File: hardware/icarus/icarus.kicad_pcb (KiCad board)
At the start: 4 copper layers, 43.7 x 42.4 mm, 32 parts, among them J1 USB_B_Micro, J2 SWJ-DP, J3 PWR, J4 PWM, J5 COMMS, J6 GPIO, SW1 RST, SW2 BOOT, U1 STM32F302C8Tx, U2 AMS1117-3.3, U3 MPU-6050, Y1 12MHz

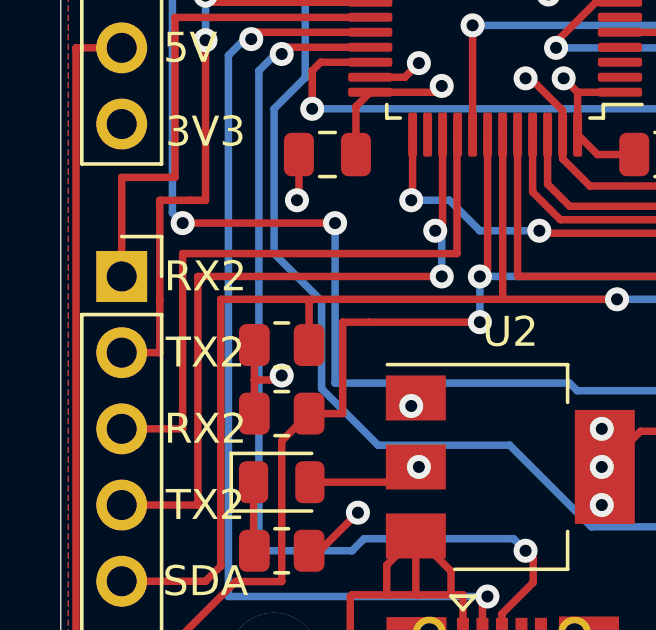
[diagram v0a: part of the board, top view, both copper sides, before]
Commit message: Resolves #2, #9, #10. Test points, USART1 Labels, IMU AD0 pint.
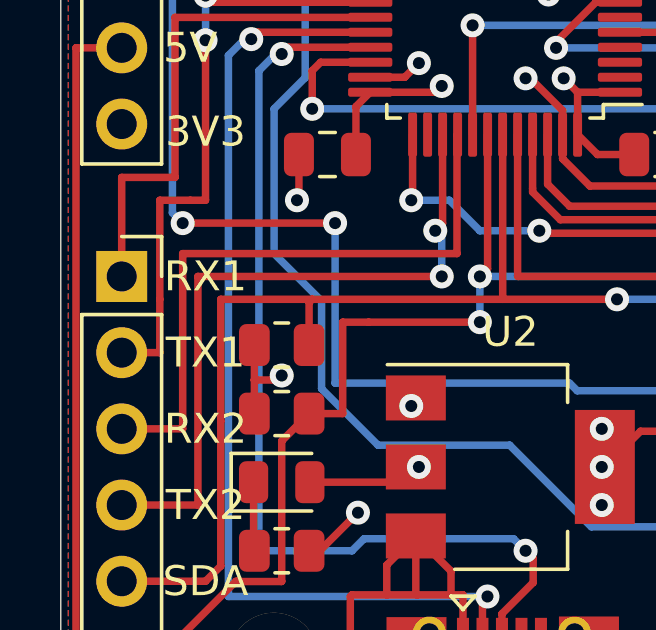
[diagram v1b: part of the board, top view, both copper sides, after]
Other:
- board text added: "RX1"
- board text added: "TX1"

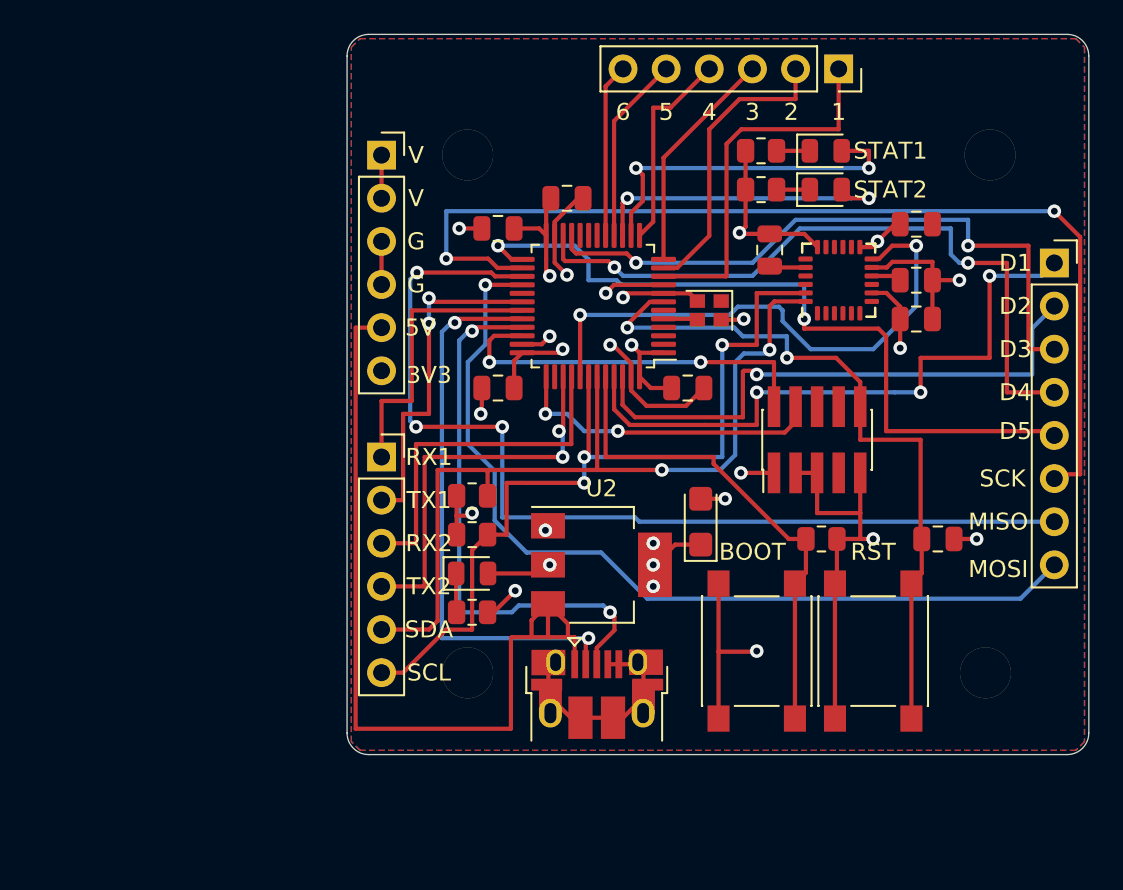
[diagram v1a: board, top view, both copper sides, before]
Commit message: Kicad 6 Update
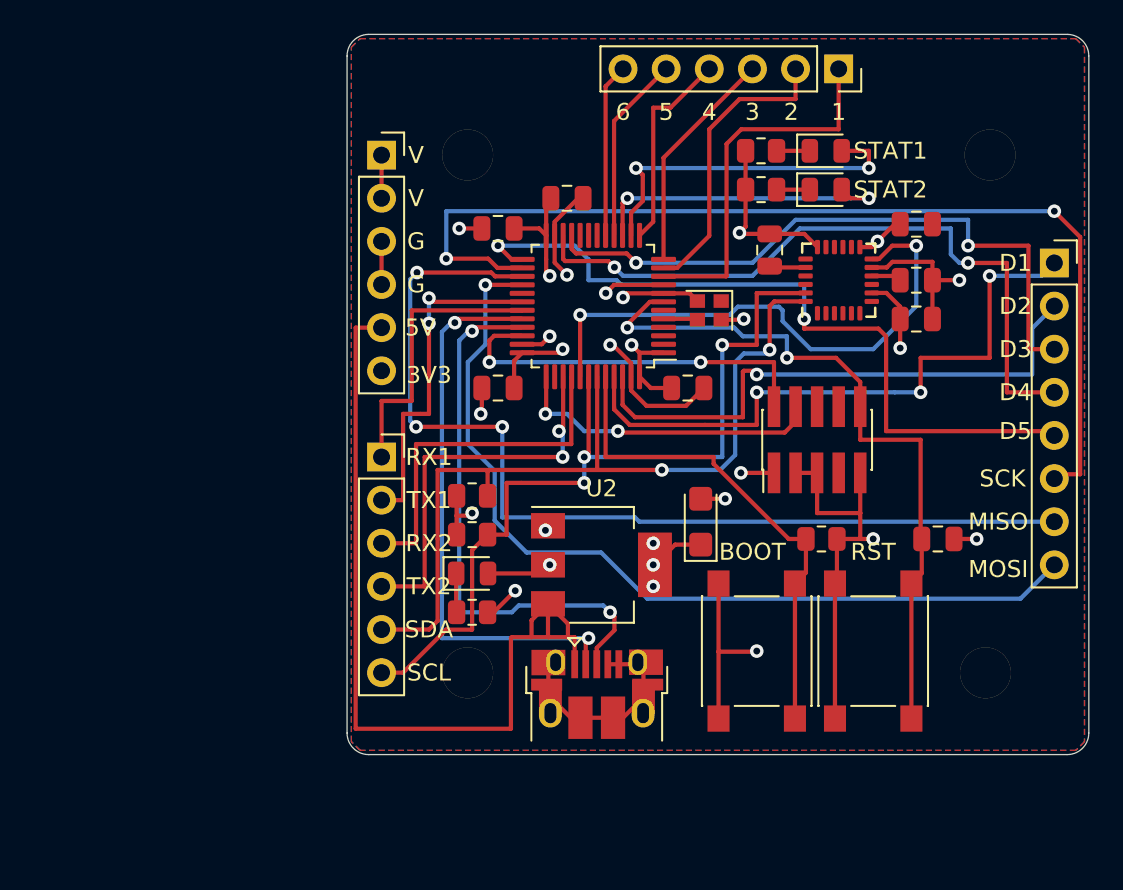
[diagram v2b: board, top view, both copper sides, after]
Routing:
- added copper zone on In1.Cu, net +3V3
- added copper zone on In2.Cu, net GND
- removed copper zone on PWR, net +3V3
- removed copper zone on GND, net GND
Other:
- net class Default removed

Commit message: Resolves #6, #17, #18. Resize and routing. Added barometer.
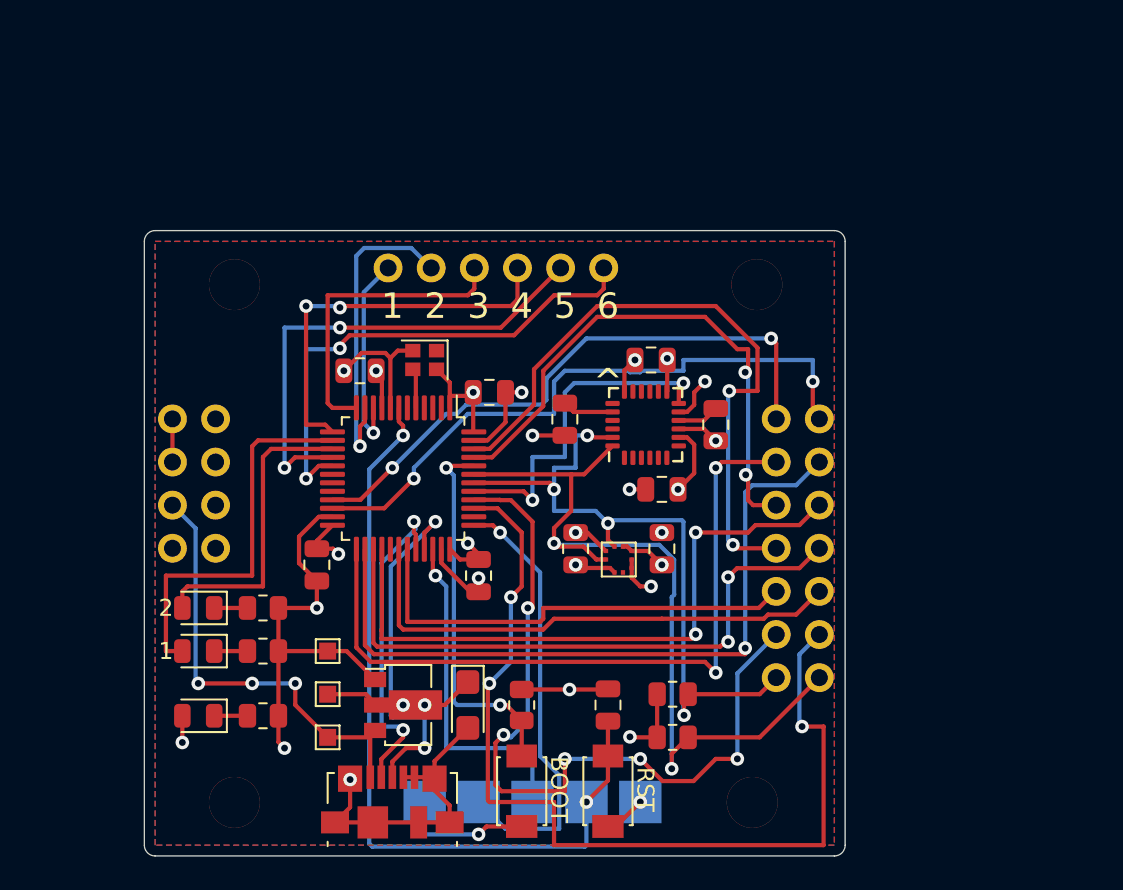
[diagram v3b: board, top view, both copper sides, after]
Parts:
- removed J3: PWR, Connector_PinSocket_2.54mm:PinSocket_1x06_P2.54mm_Vertical
- removed J4: PWM, Connector_PinSocket_2.54mm:PinSocket_1x06_P2.54mm_Vertical
- removed J5: COMMS, Connector_PinSocket_2.54mm:PinSocket_1x06_P2.54mm_Vertical
- removed J6: GPIO, Connector_PinSocket_2.54mm:PinSocket_1x08_P2.54mm_Vertical
- removed REF**: mounting_holes_30.5mm, drone:mounting_holes_30.5mm
- added C12: 100nF, Capacitor_SMD:C_0805_2012Metric, F.Cu at (162.6, 77.8)
- added C2: 100nF, Capacitor_SMD:C_0805_2012Metric, F.Cu at (167.6, 77.8)
- added TP1: 3V3, TestPoint:TestPoint_Pad_1.0x1.0mm, F.Cu at (148.0, 86.4)
- added TP2: 5V, TestPoint:TestPoint_Pad_1.0x1.0mm, F.Cu at (148.0, 88.9)
- added TP3: GND, TestPoint:TestPoint_Pad_1.0x1.0mm, F.Cu at (148.0, 83.8)
- added U4: BMP388, sensors:BMP388, F.Cu at (165.1, 78.4)
- added U5: ICARUS, icarus:icarus-shield, F.Cu at (157.9, 60.0)
- J1: footprint Connector_USB:USB_Micro-B_Amphenol_10103594-0001LF_Horizontal -> Connector_USB:USB_Micro-B_Molex_47346-0001
- J2: value SWJ-DP -> SWD; footprint Connector_PinHeader_1.27mm:PinHeader_2x05_P1.27mm_Vertical_SMD -> custom-breakout:SWD-bcu
- R2, R6, R7: value 100 -> 200
- SW1, SW2: footprint Button_Switch_SMD:SW_Push_1P1T_NO_6x6mm_H9.5mm -> tactile_switches:TS-1088-AR02016
- U2: footprint Package_TO_SOT_SMD:SOT-223-3_TabPin2 -> Package_TO_SOT_SMD:SOT-89-3
- moved D2 47.3 mm to (140.3, 83.8), turned to 180 degrees
- moved D3 44.4 mm to (140.3, 81.3), turned to 180 degrees
- moved R6 41.6 mm to (144.1, 83.8), turned to 0 degrees
- moved R7 38.3 mm to (144.1, 81.3), turned to 0 degrees
- moved J2 27.1 mm to (160.0, 92.7), turned to 0 degrees
- moved C6 26.1 mm to (147.3, 78.7), turned to -90 degrees
- moved C4 21.8 mm to (164.5, 87.0), turned to 90 degrees
- moved C10 21.6 mm to (167.6, 74.3), turned to 0 degrees
- moved C3 20.5 mm to (156.8, 79.4), turned to -90 degrees
- moved R5 20.2 mm to (159.4, 87.0), turned to 90 degrees
- moved C7 19.3 mm to (149.9, 67.3), turned to 180 degrees
- moved R3 18.5 mm to (168.3, 88.9)
- moved D1 18.2 mm to (140.3, 87.6), turned to 180 degrees
- moved SW1 17.7 mm to (164.5, 92.1)
- moved C1 17.5 mm to (156.2, 87.0), turned to -90 degrees
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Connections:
- J2 pad 2: /swdio -> /swclk
- J2 pad 3: GND -> /swdio
- J2 pad 4: /swclk -> /nreset
- U1 pad 18: Net-(U1-Pad18) -> unconnected-(U1-Pad18)
- U1 pad 19: Net-(U1-Pad19) -> unconnected-(U1-Pad19)
- U1 pad 2: Net-(U1-Pad2) -> unconnected-(U1-Pad2)
- U1 pad 20: Net-(U1-Pad20) -> unconnected-(U1-Pad20)
- U1 pad 21: /gpio3 -> /gpio1
- U1 pad 22: /gpio4 -> /gpio2
- U1 pad 25: /gpio5 -> /gpio3
- U1 pad 29: Net-(U1-Pad29) -> unconnected-(U1-Pad29)
- U1 pad 3: Net-(U1-Pad3) -> unconnected-(U1-Pad3)
- U1 pad 38: Net-(U1-Pad38) -> unconnected-(U1-Pad38)
- U1 pad 4: Net-(U1-Pad4) -> unconnected-(U1-Pad4)
- U1 pad 45: /gpio1 -> /can_rx
- U1 pad 46: /gpio2 -> /can_tx
- U3 pad 1: Net-(U3-Pad1) -> unconnected-(U3-Pad1)
- U3 pad 6: Net-(U3-Pad6) -> unconnected-(U3-Pad6)
- U3 pad 7: Net-(U3-Pad7) -> unconnected-(U3-Pad7)
- U3 pad 9: Net-(U3-Pad9) -> GND
- Y1 pad 1: Net-(Y1-Pad1) -> unconnected-(Y1-Pad1)
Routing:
- net /gpio5: track 44.7 -> 0.00 mm, vias 2 -> 0
- net /gpio4: track 41.2 -> 0.00 mm, vias 2 -> 0
- net /can_tx: track 0.00 -> 38.6 mm, vias 0 -> 2
- net /usart2_tx: track 23.3 -> 56.6 mm, vias 2 -> 3
- net /can_rx: track 0.00 -> 32.6 mm, vias 0 -> 2
- net /usart2_rx: track 21.0 -> 46.7 mm, vias 0 -> 5
- net VBUS: track 51.8 -> 26.6 mm, vias 0 -> 3
- net /miso: track 58.7 -> 36.6 mm, vias 3 -> 2
- net /pwm6: track 10.2 -> 29.8 mm, vias 0 -> 2
- net /sck: track 61.1 -> 43.0 mm, vias 2 -> 1
- net /pwm5: track 11.1 -> 29.0 mm, vias 0 -> 2
- net /mosi: track 52.8 -> 38.0 mm, vias 1 -> 2
- net /usb_fs_dm: track 33.6 -> 18.9 mm
- net /imu_int: track 32.6 -> 20.6 mm
- net /usb_fs_dp: track 33.1 -> 21.4 mm
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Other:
- board size 43.7 x 42.4 mm -> 41.3 x 36.8 mm
- board text added: "GND"
- board text added: "NRST"
- board text added: "SWCLK"
- board text added: "SWDIO"
- board text added: "^"
- board text added: "icarus :: Rev B nnarain"
- board text removed: "5V"
- board text removed: "D1"
- board text removed: "D2"
- board text removed: "D3"
- board text removed: "D4"
- board text removed: "D5"
- board text removed: "G"
- board text removed: "MISO"
- board text removed: "MOSI"
- board text removed: "RX1"
- board text removed: "RX2"
- board text removed: "SCK"
- board text removed: "SCL"
- board text removed: "SDA"
- board text removed: "TX1"
- board text removed: "TX2"
- board text removed: "V"
- board text removed: "icarus :: Rev A nnarain"

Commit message: Rev C
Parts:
- removed C11, C12: 100nF, Capacitor_SMD:C_0805_2012Metric
- removed J2: SWD, custom-breakout:SWD-bcu
- removed Y1: 12MHz, Crystal:Crystal_SMD_2016-4Pin_2.0x1.6mm
- added D4: STAT, LED_SMD:LED_WS2812B_PLCC4_5.0x5.0mm_P3.2mm, F.Cu at (140.6, 80.4)
- added D5: CHR, LED_SMD:LED_0805_2012Metric, F.Cu at (142.7, 88.4)
- added G***: LOGO, symbols:battery2_3, F.Cu at (159.9, 86.9)
- added G***: LOGO, icarus:icarus-logo, F.Cu at (136.9, 73.8)
- added G***: LOGO, symbols:charge_1x1, F.Cu at (142.7, 90.7)
- added G***: LOGO, symbols:radio1, B.Cu at (149.1, 52.6)
- added M1: RTR1, Connector_PinHeader_2.54mm:PinHeader_1x02_P2.54mm_Vertical, F.Cu at (163.3, 61.1)
- added M2: RTR2, Connector_PinHeader_2.54mm:PinHeader_1x02_P2.54mm_Vertical, F.Cu at (163.3, 81.9)
- added M3: RTR3, Connector_PinHeader_2.54mm:PinHeader_1x02_P2.54mm_Vertical, F.Cu at (135.1, 61.1)
- added M4: RTR4, Connector_PinHeader_2.54mm:PinHeader_1x02_P2.54mm_Vertical, F.Cu at (135.1, 81.9)
- added P1: USB_C_Plug_USB2.0, USB-C-Connectors:TYPE-C-31-M-04, F.Cu at (149.5, 89.5)
- added Q1: DMG2305, Package_TO_SOT_SMD:SOT-23, F.Cu at (155.2, 79.0)
- added Q2: 2N7002, Package_TO_SOT_SMD:SOT-23, F.Cu at (140.5, 64.9)
- added R1: 100k, Resistor_SMD:R_0402_1005Metric, F.Cu at (158.6, 82.2)
- added R10: 1k, Resistor_SMD:R_0402_1005Metric, F.Cu at (142.9, 85.3)
- added R11: 10k, Resistor_SMD:R_0402_1005Metric, F.Cu at (160.4, 75.7)
- added R12: 10k, Resistor_SMD:R_0402_1005Metric, F.Cu at (160.4, 72.3)
- added R13: 10k, Resistor_SMD:R_0402_1005Metric, F.Cu at (158.4, 66.0)
- added R8: 4.7k, Resistor_SMD:R_0402_1005Metric, F.Cu at (157.6, 76.2)
- added R9: 100k, Resistor_SMD:R_0402_1005Metric, F.Cu at (143.6, 67.3)
- added REF**: mounting_holes_30.5mm, drone:mounting_holes_30.5mm, F.Cu at (149.1, 71.5)
- added TP4: GND, TestPoint:TestPoint_Pad_1.0x1.0mm, F.Cu at (162.7, 91.3)
- added U6: BMP388, sensors:BMP388, F.Cu at (139.4, 57.9)
- added U7: ESP32-C3-MINI-1, Espressif:ESP32-C3-MINI-1, F.Cu at (149.1, 60.8)
- C10: value 10nF -> 100nF; footprint Capacitor_SMD:C_0805_2012Metric -> Capacitor_SMD:C_0402_1005Metric
- C2, C5, C7, C8: footprint Capacitor_SMD:C_0805_2012Metric -> Capacitor_SMD:C_0402_1005Metric
- C3: value 4.7uF -> 2.2nF; footprint Capacitor_SMD:C_0805_2012Metric -> Capacitor_SMD:C_0402_1005Metric
- C4: value 100nF -> 10nF; footprint Capacitor_SMD:C_0805_2012Metric -> Capacitor_SMD:C_0402_1005Metric
- C6: value 100nF -> 4.7uF; footprint Capacitor_SMD:C_0805_2012Metric -> Capacitor_SMD:C_0402_1005Metric
- C9: value 2.2nF -> 100nF; footprint Capacitor_SMD:C_0805_2012Metric -> Capacitor_SMD:C_0402_1005Metric
- D1: value PWR -> B5819W; footprint LED_SMD:LED_0805_2012Metric -> Diode_SMD:D_SOD-123
- D2: value STAT1 -> 5V
- D3: value STAT2 -> 3V3
- J1: value USB_B_Micro -> BAT; footprint Connector_USB:USB_Micro-B_Molex_47346-0001 -> Connector_PinHeader_2.54mm:PinHeader_1x02_P2.54mm_Vertical
- R2, R7: value 200 -> 10k; footprint Resistor_SMD:R_0805_2012Metric -> Resistor_SMD:R_0402_1005Metric
- R3: footprint Resistor_SMD:R_0805_2012Metric -> Resistor_SMD:R_0402_1005Metric
- R4: value 10k -> 1k; footprint Resistor_SMD:R_0805_2012Metric -> Resistor_SMD:R_0402_1005Metric
- R5: value 10k -> 560; footprint Resistor_SMD:R_0805_2012Metric -> Resistor_SMD:R_0402_1005Metric
- R6: value 200 -> 6.8k; footprint Resistor_SMD:R_0805_2012Metric -> Resistor_SMD:R_0402_1005Metric
- SW1: value RST -> USER
- SW2: value BOOT -> RST
- TP1: value 3V3 -> VBUS
- TP2: value 5V -> BATT
- U1: value STM32F302C8Tx -> AMS1117-3.3; footprint Package_QFP:LQFP-48_7x7mm_P0.5mm -> Package_TO_SOT_SMD:SOT-223-3_TabPin2
- U2: value AMS1117-3.3 -> DRV8837; footprint Package_TO_SOT_SMD:SOT-89-3 -> Package_SON:WSON-8-1EP_2x2mm_P0.5mm_EP0.9x1.6mm
- U3: value MPU-6050 -> DRV8837; footprint Sensor_Motion:InvenSense_QFN-24_4x4mm_P0.5mm -> Package_SON:WSON-8-1EP_2x2mm_P0.5mm_EP0.9x1.6mm
- U4: value BMP388 -> MPU-6050; footprint sensors:BMP388 -> Sensor_Motion:InvenSense_QFN-24_4x4mm_P0.5mm
- U5: value ICARUS -> MCP73831-2-OT; footprint icarus:icarus-shield -> Package_TO_SOT_SMD:SOT-23-5
- moved R3 39.9 mm to (141.6, 59.2), turned to 90 degrees
- moved C8 34.1 mm to (139.8, 56.3), turned to 180 degrees
- moved R4 29.7 mm to (138.6, 85.3), turned to 90 degrees
- moved U2 27.2 mm to (133.9, 67.1)
- moved C2 22.9 mm to (145.2, 73.4), turned to -90 degrees
- moved R6 22.6 mm to (140.4, 61.6), turned to 90 degrees
- moved C4 22.5 mm to (145.2, 75.4)
- moved R2 20.4 mm to (145.7, 67.3)
- moved SW1 20.3 mm to (164.7, 71.8), turned to 180 degrees
- moved R7 19.9 mm to (141.6, 61.6), turned to -90 degrees
- moved R5 18.7 mm to (140.7, 85.3)
- moved U4 17.4 mm to (149.1, 71.5), turned to -90 degrees
- moved SW2 16.7 mm to (164.7, 76.2), turned to 0 degrees
- moved D1 16.1 mm to (155.6, 82.3), turned to 0 degrees
- moved U5 14.9 mm to (155.2, 74.7), turned to -90 degrees
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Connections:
- C10 pad 1: GND -> /user_btn
- C10 pad 2: +3V3 -> GND
- C2 pad 1: +3V3 -> Net-(C2-Pad1)
- C3 pad 1: +3V3 -> Net-(C3-Pad1)
- C4 pad 1: /nreset -> GND
- C4 pad 2: GND -> +3V3
- C5 pad 1: +3V3 -> GND
- C5 pad 2: GND -> +3V3
- C6 pad 1: +3V3 -> +BATT
- C8 pad 1: Net-(C8-Pad1) -> +3V3
- C9 pad 1: Net-(C9-Pad1) -> /nreset
- D1 pad 2: +3V3 -> VBUS
- D2 pad 2: /led1 -> VBUS
- D3 pad 2: /led2 -> +3V3
- J1 pad 1: VBUS -> +BATT
- J1 pad 2: /usb_fs_dm -> GND
- R2 pad 1: Net-(D1-Pad1) -> /sda
- R2 pad 2: GND -> +3V3
- R3 pad 1: +3V3 -> /scl
- R3 pad 2: /sda -> +3V3
- R4 pad 1: +3V3 -> Net-(D2-Pad1)
- R4 pad 2: /scl -> GND
- R5 pad 1: /boot0 -> Net-(D3-Pad1)
- R6 pad 1: Net-(D2-Pad1) -> +BATT
- R6 pad 2: GND -> Net-(R6-Pad2)
- R7 pad 1: Net-(D3-Pad1) -> Net-(R6-Pad2)
- SW1 pad 1: /nreset -> GND
- SW1 pad 2: GND -> /user_btn
- SW2 pad 1: /boot0 -> /nreset
- SW2 pad 2: +3V3 -> GND
- TP1 pad 1: +3V3 -> VBUS
- TP2 pad 1: VBUS -> +BATT
- TP3 pad 1: GND -> +3V3
- U1 pad 1: +3V3 -> GND
- U1 pad 2: unconnected-(U1-Pad2) -> +3V3
- U1 pad 3: unconnected-(U1-Pad3) -> Net-(D1-Pad1)
- U2 pad 1: GND -> +BATT
- U2 pad 2: +3V3 -> Net-(M4-Pad2)
- U2 pad 3: VBUS -> Net-(M3-Pad2)
- U3 pad 1: unconnected-(U3-Pad1) -> +BATT
- U3 pad 2: (no net) -> Net-(M2-Pad2)
- U3 pad 3: (no net) -> Net-(M1-Pad2)
- U3 pad 4: (no net) -> GND
- U3 pad 5: (no net) -> /rtrctl1
- U3 pad 6: unconnected-(U3-Pad6) -> /rtrctl2
- U3 pad 7: unconnected-(U3-Pad7) -> Net-(U3-Pad7)
- U4 pad 1: +3V3 -> unconnected-(U4-Pad1)
- U4 pad 10: +3V3 -> Net-(C2-Pad1)
- U4 pad 2: /scl -> (no net)
- U4 pad 3: GND -> (no net)
- U4 pad 4: /sda -> (no net)
- U4 pad 5: +3V3 -> (no net)
- U4 pad 6: +3V3 -> unconnected-(U4-Pad6)
- U4 pad 8: GND -> +3V3
- U5 pad 1: VDC -> Net-(D5-Pad1)
- U5 pad 3: VDC -> +BATT
- U5 pad 4: GND -> VBUS
- U5 pad 5: VBUS -> Net-(R8-Pad1)
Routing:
- net Net-(D5-Pad1): track 0.00 -> 71.9 mm, vias 0 -> 8
- net /usart2_tx: track 56.6 -> 0.00 mm, vias 3 -> 0
- net Net-(D4-Pad4): track 0.00 -> 47.3 mm, vias 0 -> 2
- net /usb_dm: track 0.00 -> 47.2 mm, vias 0 -> 4
- net /usart2_rx: track 46.7 -> 0.00 mm, vias 5 -> 0
- net /usb_dp: track 0.00 -> 45.2 mm, vias 0 -> 4
- net /gpio3: track 43.3 -> 0.00 mm, vias 2 -> 0
- net /sck: track 43.0 -> 0.00 mm, vias 1 -> 0
- net /can_tx: track 38.6 -> 0.00 mm, vias 2 -> 0
- net /mosi: track 38.0 -> 0.00 mm, vias 2 -> 0
- net /gpio2: track 37.5 -> 0.00 mm, vias 2 -> 0
- net /miso: track 36.6 -> 0.00 mm, vias 2 -> 0
- net VBUS: track 26.6 -> 62.3 mm, vias 3 -> 0
- net /gpio1: track 35.4 -> 0.00 mm, vias 2 -> 0
- net /can_rx: track 32.6 -> 0.00 mm, vias 2 -> 0
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- added copper zone on In1.Cu, net +BATT
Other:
- board size 41.3 x 36.8 mm -> 37.1 x 43.3 mm
- board text added: "B"
- board text added: "G"
- board text added: "RST"
- board text added: "U"
- board text added: "USER"
- board text added: "icarus :: Rev C nnarain"
- board text removed: "1"
- board text removed: "2"
- board text removed: "3V3"
- board text removed: "4"
- board text removed: "5"
- board text removed: "6"
- board text removed: "GND"
- board text removed: "NRST"
- board text removed: "SWCLK"
- board text removed: "SWDIO"
- board text removed: "^"
- board text removed: "icarus :: Rev B nnarain"

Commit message: Rev D
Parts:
- removed C6: 4.7uF, Capacitor_SMD:C_0402_1005Metric
- removed D5: CHR, LED_SMD:LED_0805_2012Metric
- removed the G*** at (142.7, 90.7)
- removed M1: RTR1, Connector_PinHeader_2.54mm:PinHeader_1x02_P2.54mm_Vertical
- removed M2: RTR2, Connector_PinHeader_2.54mm:PinHeader_1x02_P2.54mm_Vertical
- removed M3: RTR3, Connector_PinHeader_2.54mm:PinHeader_1x02_P2.54mm_Vertical
- removed M4: RTR4, Connector_PinHeader_2.54mm:PinHeader_1x02_P2.54mm_Vertical
- removed Q2: 2N7002, Package_TO_SOT_SMD:SOT-23
- removed R10: 1k, Resistor_SMD:R_0402_1005Metric
- removed R7: 10k, Resistor_SMD:R_0402_1005Metric
- removed R8: 4.7k, Resistor_SMD:R_0402_1005Metric
- removed R9: 100k, Resistor_SMD:R_0402_1005Metric
- removed U3: DRV8837, Package_SON:WSON-8-1EP_2x2mm_P0.5mm_EP0.9x1.6mm
- removed U5: MCP73831-2-OT, Package_TO_SOT_SMD:SOT-23-5
- added J2: IO, Connector_PinHeader_2.54mm:PinHeader_1x06_P2.54mm_Vertical, F.Cu at (132.7, 65.2)
- added J3: I2C_EX, Connector_PinHeader_2.54mm:PinHeader_1x02_P2.54mm_Vertical, F.Cu at (164.5, 61.0)
- added J4: UART, Connector_PinHeader_2.54mm:PinHeader_1x02_P2.54mm_Vertical, F.Cu at (164.5, 67.3)
- R6: value 6.8k -> 10k
- U2: value DRV8837 -> BMM150; footprint Package_SON:WSON-8-1EP_2x2mm_P0.5mm_EP0.9x1.6mm -> Package_CSP:WLCSP-12_1.56x1.56mm_P0.4mm
- moved U2 21.2 mm to (154.6, 71.5), turned to 180 degrees
- moved R6 18.8 mm to (156.3, 71.5), turned to -90 degrees
- moved C9 6.00 mm to (160.7, 82.8)
- moved R11 6.00 mm to (160.7, 81.7)
- moved SW2 5.84 mm to (164.7, 82.0)
- moved R13 5.34 mm to (153.3, 67.7)
- moved C10 5.23 mm to (159.9, 76.3)
- moved R12 5.23 mm to (159.9, 77.5)
- moved SW1 5.08 mm to (164.7, 76.8)
- moved G*** 4.50 mm to (140.3, 70.9), turned to 90 degrees
- moved C2 1.85 mm to (145.7, 71.6)
- moved C4 1.85 mm to (145.7, 73.7)
- moved C5 1.85 mm to (145.7, 69.6)
- moved D3 1.73 mm to (142.4, 88.4)
- moved R5 1.65 mm to (142.4, 85.3)
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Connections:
- net /rtrctl1 renamed Net-(R13-Pad2)
- R6 pad 1: +BATT -> +3V3
- U7 pad 12: Net-(Q2-Pad2) -> Net-(D4-Pad4)
- U7 pad 16: /drv1_en -> /io2
- U7 pad 18: /rtrctl4 -> /io3
- U7 pad 19: /rtrctl3 -> /io4
- U7 pad 20: Net-(U3-Pad7) -> /io5
- U7 pad 21: /rtrctl2 -> /io6
- U7 pad 30: unconnected-(U7-Pad30) -> Net-(J4-Pad2)
- U7 pad 31: Net-(D4-Pad4) -> Net-(J4-Pad1)
- U7 pad 6: Net-(R6-Pad2) -> /io1
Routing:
- net Net-(D5-Pad1): track 71.9 -> 0.00 mm, vias 8 -> 0
- net /sda: track 30.3 -> 61.1 mm, vias 6 -> 8
- net Net-(D4-Pad4): track 47.3 -> 18.6 mm, vias 2 -> 0
- net /io6: track 0.00 -> 26.7 mm, vias 0 -> 1
- net /io5: track 0.00 -> 22.9 mm, vias 0 -> 1
- net /scl: track 27.4 -> 50.0 mm, vias 4 -> 5
- net /io4: track 0.00 -> 21.1 mm, vias 0 -> 1
- net /rtrctl3: track 20.3 -> 0.00 mm, vias 2 -> 0
- net /io3: track 0.00 -> 19.1 mm, vias 0 -> 1
- net /rtrctl4: track 18.4 -> 0.00 mm
- net Net-(M4-Pad2): track 17.6 -> 0.00 mm, vias 2 -> 0
- net /drv1_en: track 17.5 -> 0.00 mm
- net Net-(M2-Pad2): track 17.1 -> 0.00 mm
- net /io2: track 0.00 -> 16.7 mm, vias 0 -> 1
- net +BATT: track 30.5 -> 14.2 mm, vias 5 -> 1
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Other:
- rule pad_to_mask_clearance: 0 -> 0.05
- board text added: "1"
- board text added: "2"
- board text added: "4"
- board text added: "5"
- board text added: "6"
- board text added: "RX"
- board text added: "SCL"
- board text added: "SDA"
- board text added: "TX"
- board text added: "^"
- board text added: "icarus :: Rev D nnarain"
- board text removed: "U"
- board text removed: "icarus :: Rev C nnarain"
